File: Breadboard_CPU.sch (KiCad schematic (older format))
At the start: 0 parts

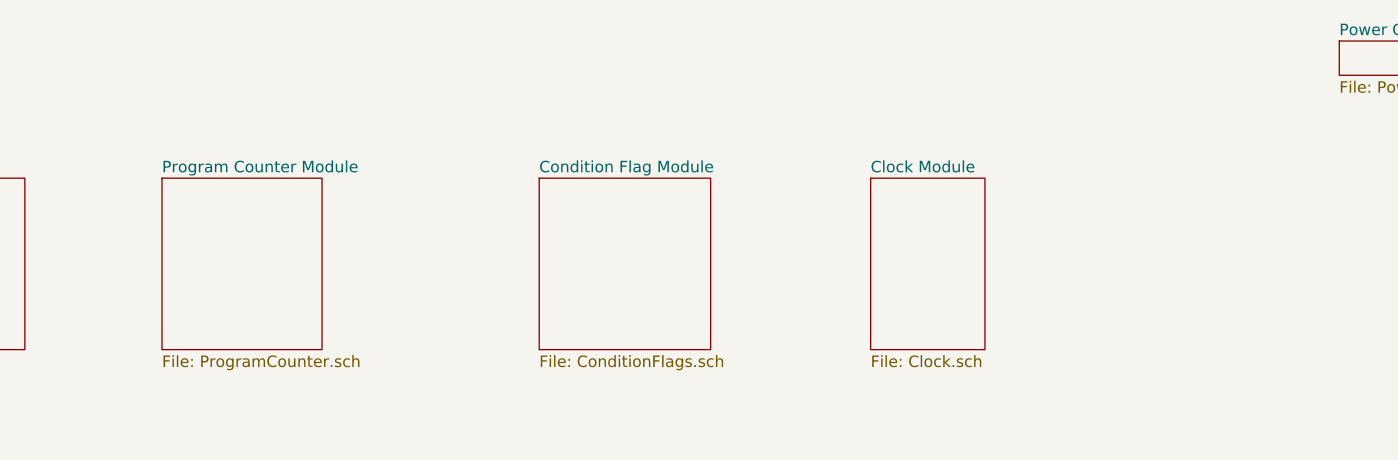
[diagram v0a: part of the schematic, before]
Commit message: Added clock and program counter modules.  Refined some schematics.
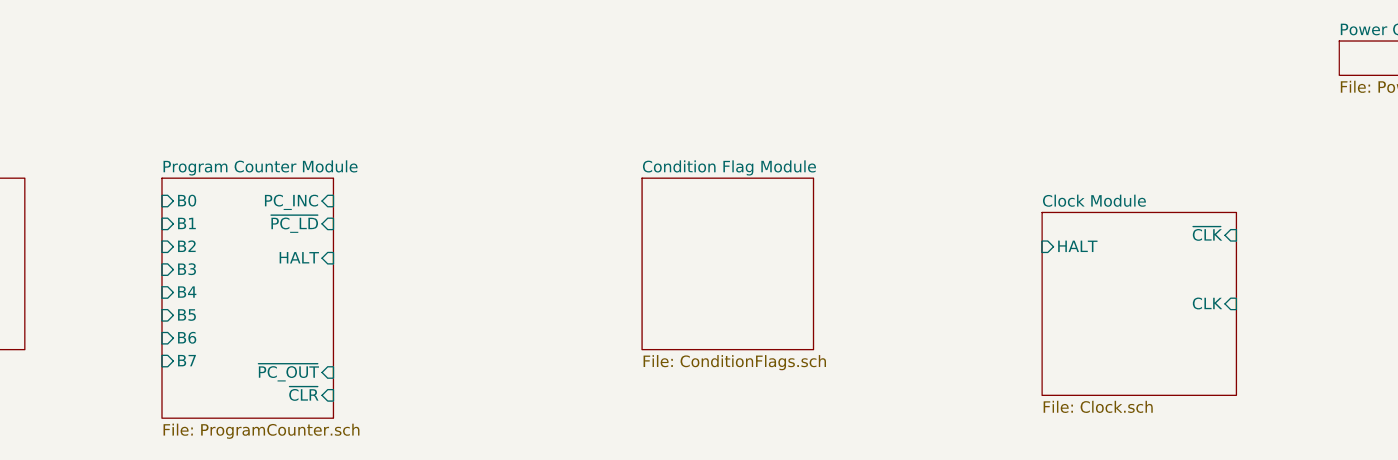
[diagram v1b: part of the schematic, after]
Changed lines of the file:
@@
 EELAYER 30 0
 EELAYER END
-$Descr A4 11693 8268
+$Descr A2 23386 16535
 encoding utf-8
 Sheet 1 8
@@
 $EndSheet
 $Sheet
-S 4900 1200 700  750
+S 4900 1200 750  1050
 U 5EFC0772
 F0 "Program Counter Module" 50
 F1 "ProgramCounter.sch" 50
+F2 "B0" I L 4900 1300 50
+F3 "B1" I L 4900 1400 50
+F4 "B2" I L 4900 1500 50
+F5 "B3" I L 4900 1600 50
+F6 "B4" I L 4900 1700 50
+F7 "B5" I L 4900 1800 50
+F8 "B6" I L 4900 1900 50
+F9 "B7" I L 4900 2000 50
+F10 "PC_INC" I R 5650 1300 50
+F11 "~PC_LD" I R 5650 1400 50
+F12 "~CLR" I R 5650 2150 50
+F13 "~PC_OUT" I R 5650 2050 50
+F14 "HALT" I R 5650 1550 50
 $EndSheet
 $Sheet
-S 6550 1200 750  750
+S 7000 1200 750  750
 U 5EFC0970
 F0 "Condition Flag Module" 50
@@
 $EndSheet
 $Sheet
-S 8000 1200 500  750
+S 8750 1350 850  800
 U 5EFC09F3
 F0 "Clock Module" 50
 F1 "Clock.sch" 50
+F2 "HALT" I L 8750 1500 50
+F3 "CLK" I R 9600 1750 50
+F4 "~CLK" I R 9600 1450 50
 $EndSheet
 $Sheet

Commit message: Continued work.  Pushing for remote work.
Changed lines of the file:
@@
 EELAYER 30 0
 EELAYER END
-$Descr A2 23386 16535
+$Descr A3 16535 11693
 encoding utf-8
-Sheet 1 8
+Sheet 1 9
 Title ""
 Date ""
@@
 $EndDescr
 $Sheet
-S 2550 1200 700  750
-U 5EFC0623
-F0 "Memory Module" 50
-F1 "Memory.sch" 50
-$EndSheet
-$Sheet
-S 1400 1200 750  750
+S 7000 1450 850  900
 U 5EFC04D0
 F0 "Registers Module" 50
 F1 "Registers.sch" 50
+F2 "B0" B L 7000 1550 50
+F3 "B1" B L 7000 1650 50
+F4 "B2" B L 7000 1750 50
+F5 "B3" B L 7000 1850 50
+F6 "B4" B L 7000 1950 50
+F7 "B5" B L 7000 2050 50
+F8 "B6" B L 7000 2150 50
+F9 "B7" B L 7000 2250 50
+F10 "~CLK" I R 7850 2150 50
+F11 "~REG_IN" I R 7850 2050 50
+F12 "~REG_OUT" I R 7850 1950 50
+F13 "RS0" I R 7850 1550 50
+F14 "RS1" I R 7850 1650 50
+F15 "RS2" I R 7850 1750 50
 $EndSheet
 $Sheet
-S 3750 1200 550  750
+S 1400 1650 550  750
 U 5EFC06D4
 F0 "ALU Module" 50
@@
 $EndSheet
 $Sheet
-S 7000 1200 750  750
+S 2750 3850 750  750
 U 5EFC0970
 F0 "Condition Flag Module" 50
@@
 $EndSheet
 $Sheet
-S 8750 1350 850  800
+S 10200 2050 750  500
 U 5EFC09F3
 F0 "Clock Module" 50
 F1 "Clock.sch" 50
-F2 "HALT" I L 8750 1500 50
-F3 "CLK" I R 9600 1750 50
-F4 "~CLK" I R 9600 1450 50
+F2 "CLK" I R 10950 2450 50
+F3 "~CLK" I R 10950 2150 50
+F4 "HALT_A" I L 10200 2200 50
+F5 "HALT_B" I L 10200 2300 50
 $EndSheet
 $Sheet
@@
 $EndSheet
 $Sheet
-S 4900 1200 750  1050
+S 5050 2450 1200 1050
 U 5EFC0772
 F0 "Program Counter Module" 50
 F1 "ProgramCounter.sch" 50
-F2 "B0" I L 4900 1300 50
-F3 "B1" I L 4900 1400 50
-F4 "B2" I L 4900 1500 50
-F5 "B3" I L 4900 1600 50
-F6 "B4" I L 4900 1700 50
-F7 "B5" I L 4900 1800 50
-F8 "B6" I L 4900 1900 50
-F9 "B7" I L 4900 2000 50
-F10 "PC_INC" I R 5650 1300 50
-F11 "~PC_LD" I R 5650 1400 50
-F12 "~CLR" I R 5650 2150 50
-F13 "~PC_OUT" I R 5650 2050 50
-F14 "HALT" I R 5650 1550 50
+F2 "B0" B R 6250 3400 50
+F3 "B1" B R 6250 3300 50
+F4 "B2" B R 6250 3200 50
+F5 "B3" B R 6250 3100 50
+F6 "B4" B R 6250 3000 50
+F7 "B5" B R 6250 2900 50
+F8 "B6" B R 6250 2800 50
+F9 "B7" B R 6250 2700 50
+F10 "PC_INC" I L 5050 3400 50
+F11 "~CLR" I L 5050 2550 50
+F12 "~PC_OUT" I L 5050 2650 50
+F13 "CLK" I L 5050 2950 50
+F14 "~PC_IN" I L 5050 3300 50
+F15 "TR_HALT" O L 5050 3150 50
+$EndSheet
+$Sheet
+S 7000 2600 850  2100
+U 5EFC0623
+F0 "Memory Module" 50
+F1 "Memory.sch" 50
+F2 "B0" I L 7000 2700 50
+F3 "B1" I L 7000 2800 50
+F4 "B2" I L 7000 2900 50
+F5 "B3" I L 7000 3000 50
+F6 "B4" I L 7000 3100 50
+F7 "B5" I L 7000 3200 50
+F8 "B6" I L 7000 3300 50
+F9 "B7" I L 7000 3400 50
+F10 "~RST" I L 7000 4500 50
+F11 "CLK" I L 7000 3850 50
+F12 "MAR_IN" I L 7000 3750 50
+F13 "INTERRUPT" I L 7000 4350 50
+F14 "~MEM_OUT" I L 7000 3650 50
+F15 "I8" O R 7850 3500 50
+F16 "I9" O R 7850 3600 50
+F17 "I10" O R 7850 3700 50
+F18 "I11" O R 7850 3800 50
+F19 "I12" O R 7850 3900 50
+F20 "I13" O R 7850 4000 50
+F21 "I14" O R 7850 4100 50
+F22 "I15" O R 7850 4200 50
+F23 "I7" O R 7850 3400 50
+F24 "I6" O R 7850 3300 50
+F25 "I5" O R 7850 3200 50
+F26 "I4" O R 7850 3100 50
+F27 "I3" O R 7850 3000 50
+F28 "I2" O R 7850 2900 50
+F29 "I1" O R 7850 2800 50
+F30 "I0" O R 7850 2700 50
+F31 "MEM_IN" I L 7000 3550 50
+F32 "ETI_RTI" I L 7000 4200 50
+F33 "RST" I L 7000 4600 50
+F34 "STKPTR_INC" I L 7000 4000 50
+F35 "STKPTR_DEC" I L 7000 4100 50
+$EndSheet
+$Sheet
+S 8100 2600 1000 1750
+U 5F05F116
+F0 "Control Unit Module" 50
+F1 "ControlUnit.sch" 50
 $EndSheet
 $EndSCHEMATC

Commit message: Remote work
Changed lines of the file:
@@
 $EndSheet
 $Sheet
-S 1400 1650 550  750
+S 5300 4550 950  1250
 U 5EFC06D4
 F0 "ALU Module" 50
 F1 "ALU.sch" 50
+F2 "OVERFLOW" O L 5300 4950 50
+F3 "B0" I R 6250 5350 50
+F4 "B1" I R 6250 5250 50
+F5 "B2" I R 6250 5150 50
+F6 "B3" I R 6250 5050 50
+F7 "B4" I R 6250 4950 50
+F8 "B5" I R 6250 4850 50
+F9 "B6" I R 6250 4750 50
+F10 "B7" I R 6250 4650 50
+F11 "CLK" I L 5300 4650 50
+F12 "REGA_IN" I R 6250 5700 50
+F13 "~ALU_OUT" I R 6250 5600 50
+F14 "ALU_SAVE" I R 6250 5500 50
+F15 "OPC0" I L 5300 5700 50
+F16 "OPC1" I L 5300 5600 50
+F17 "OPC2" I L 5300 5500 50
 $EndSheet
 $Sheet
-S 2750 3850 750  750
+S 5250 3450 950  750
 U 5EFC0970
-F0 "Condition Flag Module" 50
+F0 "Conditions Module" 50
 F1 "ConditionFlags.sch" 50
 $EndSheet
 $Sheet
-S 10200 2050 750  500
+S 9600 1700 750  500
 U 5EFC09F3
 F0 "Clock Module" 50
 F1 "Clock.sch" 50
-F2 "CLK" I R 10950 2450 50
-F3 "~CLK" I R 10950 2150 50
-F4 "HALT_A" I L 10200 2200 50
-F5 "HALT_B" I L 10200 2300 50
+F2 "CLK" I L 9600 1800 50
+F3 "~CLK" I L 9600 2100 50
+F4 "HALT_A" I R 10350 2050 50
+F5 "HALT_B" I R 10350 1950 50
 $EndSheet
 $Sheet
-S 10050 600  500  150
+S 11100 1650 500  150
 U 5EFC0AE0
 F0 "Power Control Module" 50
@@
 $EndSheet
 $Sheet
-S 5050 2450 1200 1050
+S 5000 2100 1200 1050
 U 5EFC0772
 F0 "Program Counter Module" 50
 F1 "ProgramCounter.sch" 50
-F2 "B0" B R 6250 3400 50
-F3 "B1" B R 6250 3300 50
-F4 "B2" B R 6250 3200 50
-F5 "B3" B R 6250 3100 50
-F6 "B4" B R 6250 3000 50
-F7 "B5" B R 6250 2900 50
-F8 "B6" B R 6250 2800 50
-F9 "B7" B R 6250 2700 50
-F10 "PC_INC" I L 5050 3400 50
-F11 "~CLR" I L 5050 2550 50
-F12 "~PC_OUT" I L 5050 2650 50
-F13 "CLK" I L 5050 2950 50
-F14 "~PC_IN" I L 5050 3300 50
-F15 "TR_HALT" O L 5050 3150 50
+F2 "B0" B R 6200 3050 50
+F3 "B1" B R 6200 2950 50
+F4 "B2" B R 6200 2850 50
+F5 "B3" B R 6200 2750 50
+F6 "B4" B R 6200 2650 50
+F7 "B5" B R 6200 2550 50
+F8 "B6" B R 6200 2450 50
+F9 "B7" B R 6200 2350 50
+F10 "PC_INC" I L 5000 3050 50
+F11 "~CLR" I L 5000 2200 50
+F12 "~PC_OUT" I L 5000 2300 50
+F13 "CLK" I L 5000 2600 50
+F14 "~PC_IN" I L 5000 2950 50
+F15 "TR_HALT" O L 5000 2800 50
 $EndSheet
 $Sheet

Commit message: For desktop work
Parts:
- added D14, D15, D16, D17, D18, D19, D20, D21: Blue, symbol Device:LED
- added Q?: Q_NPN_CBE, symbol Device:Q_NPN_CBE
- added R100, R101, R102, R103, R104, R105, R106, R99: 4.7k, symbol Device:R
- added R? (x2): 10k, symbol Device:R
- added SW?: RESET, symbol Switch:SW_Push
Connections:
- net ALU Module/B0: now also R106.2
- net ALU Module/B1: now also R105.2
- net ALU Module/B2: now also R104.2
- net ALU Module/B3: now also R103.2
- net ALU Module/B4: now also R102.2
- net ALU Module/B5: now also R101.2
- net ALU Module/B6: now also R100.2
- net ALU Module/B7: now also R99.2
- net Clock Module/HALT_A: now also Q?.2 (B), R?.1, SW?.2
- net Memory Module/~RST: now also Q?.1 (C), R?.2
- new net: D21.2 (A), R106.1
- new net: D20.2 (A), R105.1
- new net: D19.2 (A), R104.1
- new net: D18.2 (A), R103.1
- new net: D17.2 (A), R102.1
- new net: D16.2 (A), R101.1
- new net: D15.2 (A), R100.1
- new net: D14.2 (A), R99.1
- new net GND: D14.1 (K), D15.1 (K), D16.1 (K), D17.1 (K), D18.1 (K), D19.1 (K), D20.1 (K), D21.1 (K), Q?.3 (E), R?.2
- new net VCC: R?.1, SW?.1

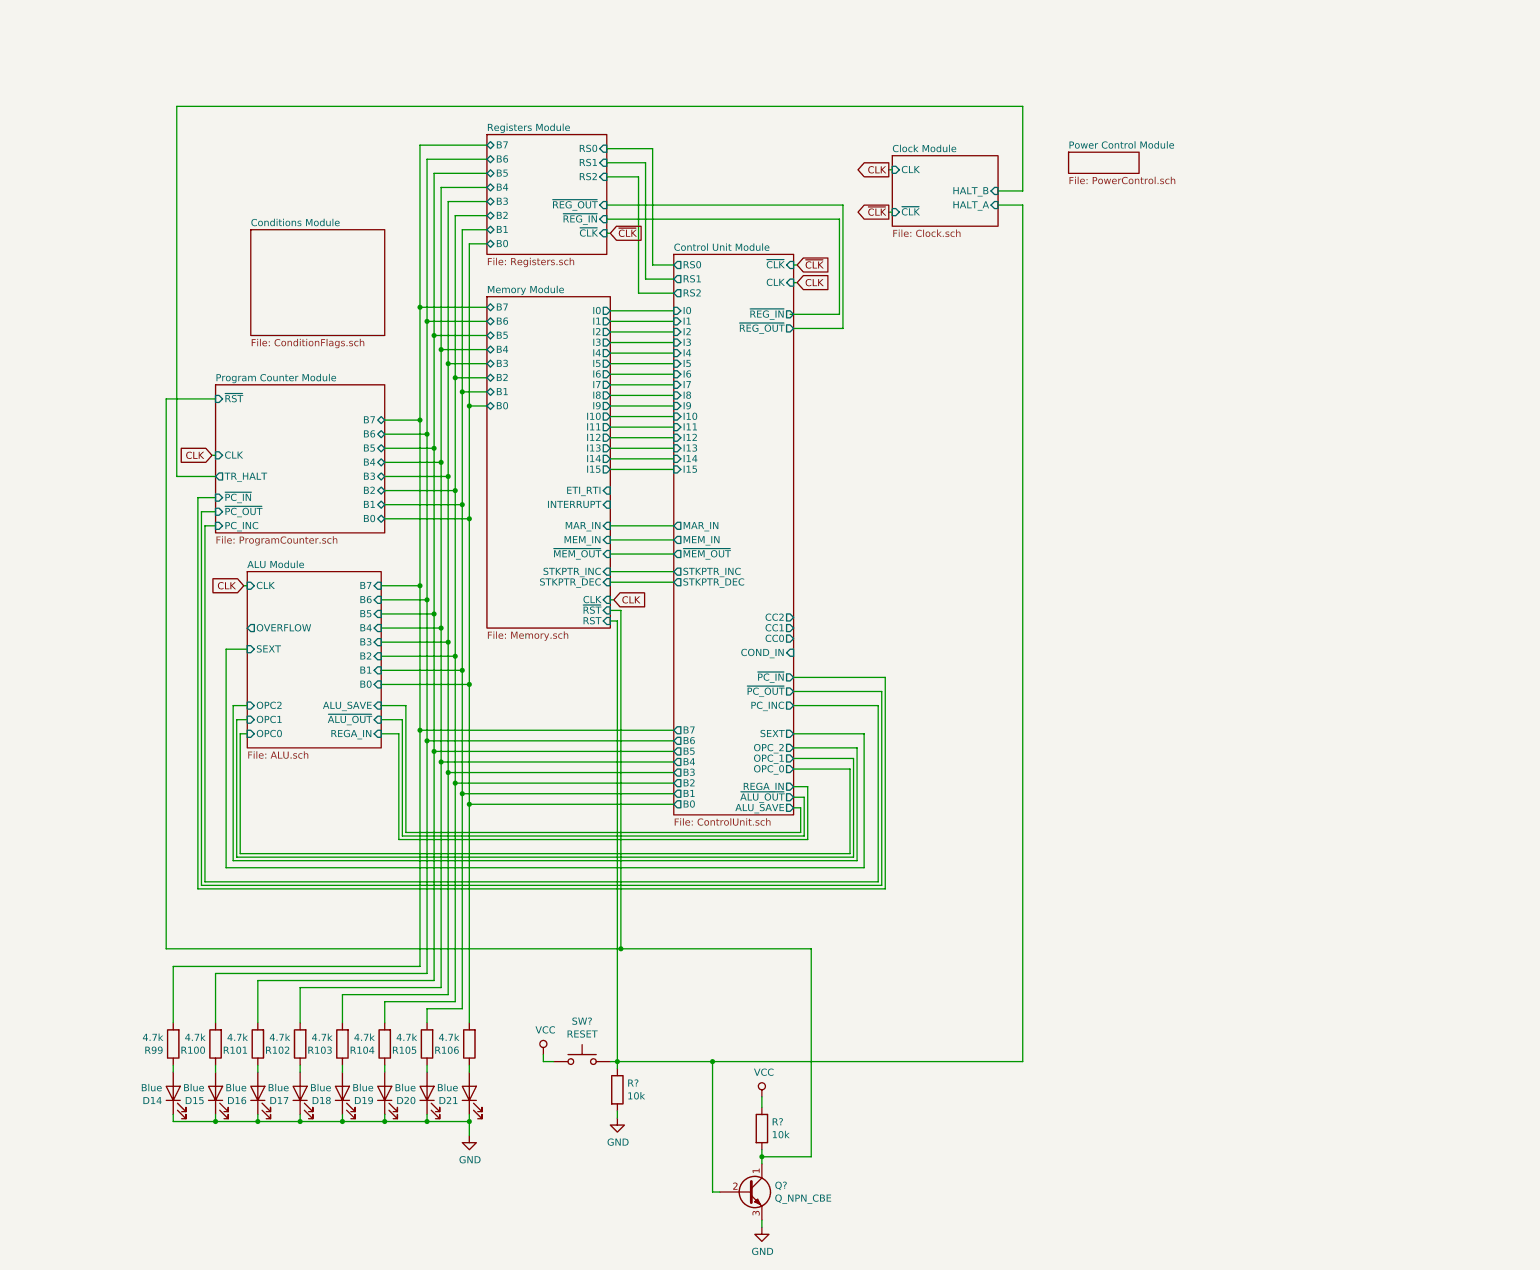
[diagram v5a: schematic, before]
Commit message: Migrated old device part numbers to SN74 LS or HCT series
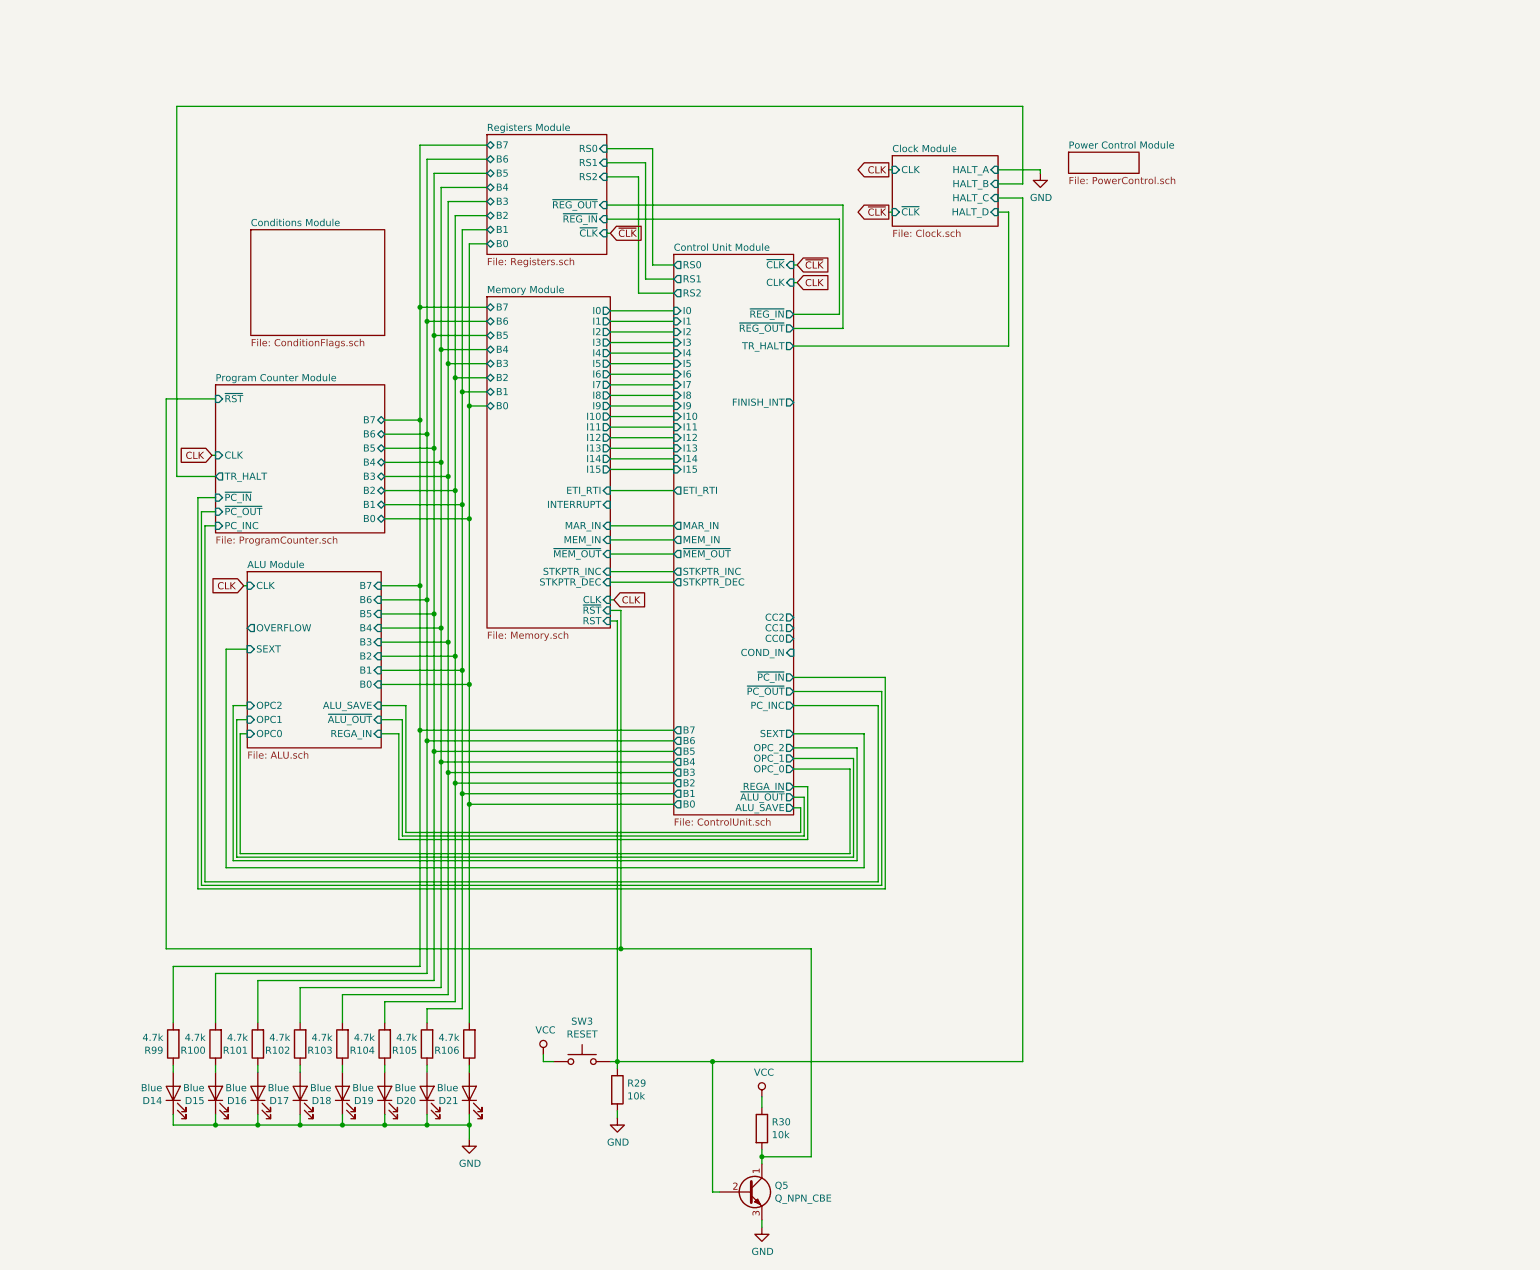
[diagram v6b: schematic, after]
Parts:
- gave numbers to parts that had none: 4
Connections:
- net Clock Module/HALT_A renamed Clock Module/HALT_C

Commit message: Remote work
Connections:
- net Memory Module/~RST renamed Control Unit Module/~RST
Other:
- note added: "Bus LEDs"
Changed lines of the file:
@@
 $EndSheet
 $Sheet
-S 3100 2050 950  750
+S 3100 1775 950  750
 U 5EFC0970
 F0 "Conditions Module" 50
@@
 $EndSheet
 $Sheet
-S 4775 2525 875  2350
+S 4775 2525 875  2375
 U 5EFC0623
 F0 "Memory Module" 50
@@
 F10 "CLK" I R 5650 4675 50
 F11 "MAR_IN" I R 5650 4150 50
-F12 "INTERRUPT" I R 5650 4000 50
+F12 "INT" I R 5650 4000 50
 F13 "~MEM_OUT" I R 5650 4350 50
 F14 "I8" O R 5650 3225 50
@@
 F52 "TR_HALT" O R 6950 2875 50
 F53 "ETI_RTI" O L 6100 3900 50
-F54 "FINISH_INT" O R 6950 3275 50
+F54 "~RST" I L 6100 4750 50
+F55 "~INT_REQ" I R 6950 4000 50
+F56 "INT" O L 6100 4000 50
 $EndSheet
 Wire Wire Line
@@
 Wire Wire Line
 	5650 3900 6100 3900
+Connection ~ 5725 4750
+Wire Wire Line
+	5725 4750 6100 4750
+Text Notes 3225 8675 0    118  ~ 0
+Bus LEDs
+Wire Wire Line
+	6100 4000 5650 4000
 $EndSCHEMATC

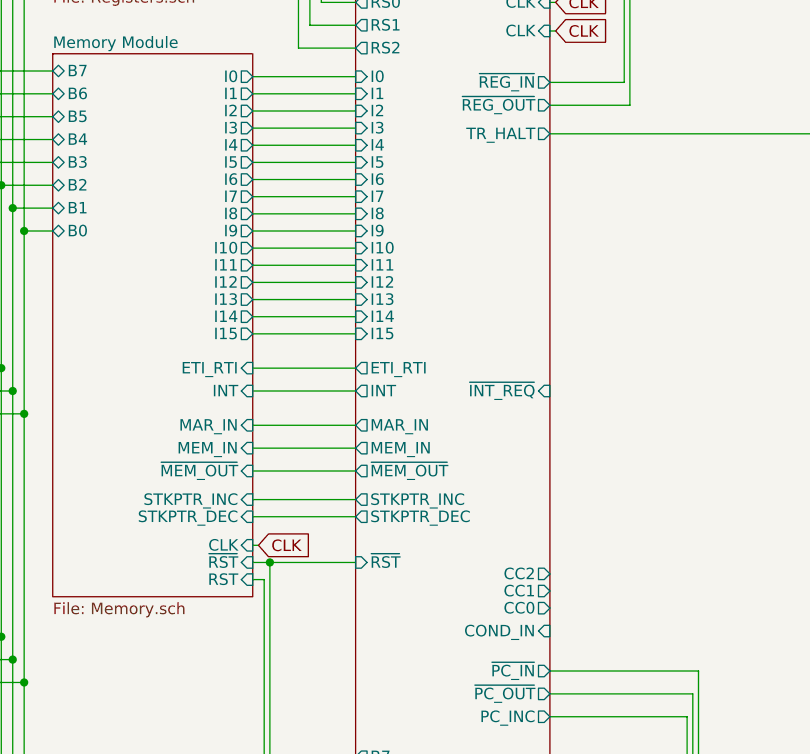
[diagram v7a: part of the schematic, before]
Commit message: Finished int handler (CPU side) and started flags module
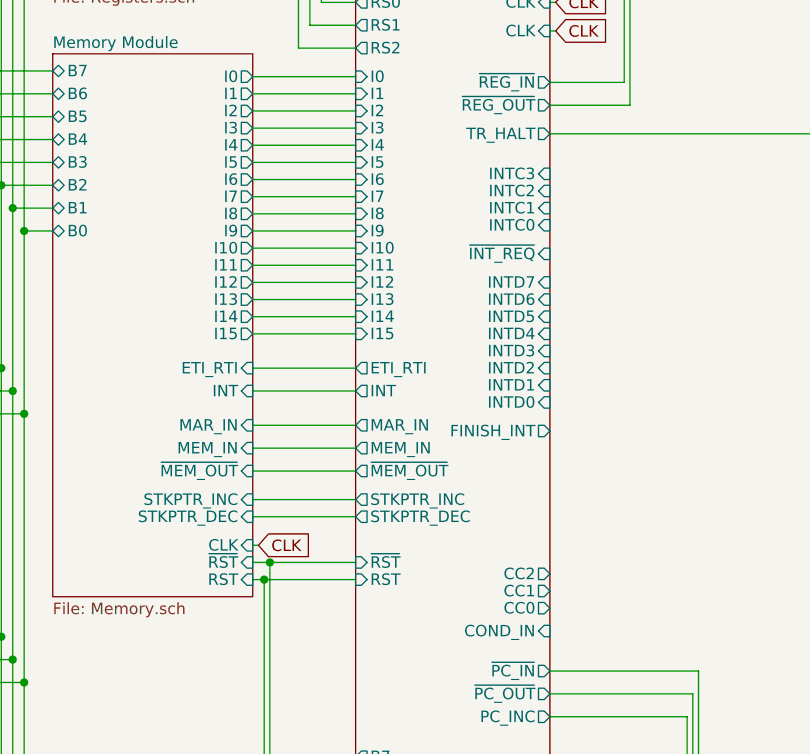
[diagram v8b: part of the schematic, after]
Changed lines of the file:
@@
 F53 "ETI_RTI" O L 6100 3900 50
 F54 "~RST" I L 6100 4750 50
-F55 "~INT_REQ" I R 6950 4000 50
+F55 "~INT_REQ" I R 6950 3400 50
 F56 "INT" O L 6100 4000 50
+F57 "INTC0" I R 6950 3275 50
+F58 "INTC1" I R 6950 3200 50
+F59 "INTC2" I R 6950 3125 50
+F60 "INTC3" I R 6950 3050 50
+F61 "RST" I L 6100 4825 50
+F62 "INTD0" I R 6950 4050 50
+F63 "INTD1" I R 6950 3975 50
+F64 "INTD2" I R 6950 3900 50
+F65 "INTD3" I R 6950 3825 50
+F66 "INTD4" I R 6950 3750 50
+F67 "INTD5" I R 6950 3675 50
+F68 "INTD6" I R 6950 3600 50
+F69 "INTD7" I R 6950 3525 50
+F70 "FINISH_INT" O R 6950 4175 50
 $EndSheet
 Wire Wire Line
@@
 Wire Wire Line
 	6100 4000 5650 4000
+Wire Wire Line
+	5700 4825 6100 4825
+Connection ~ 5700 4825
 $EndSCHEMATC
